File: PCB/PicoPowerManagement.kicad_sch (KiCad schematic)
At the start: 17 parts, among them J1 UART Header, J2 DEBUG, J3 SwitchLEDS, J4 PowerSwitch, J5 NAS Fan 1, J6 NAS Fan 2, J7 ATX 24P Connection, Q1 2N3904, U2 LP5810ADSDR, U3 LP5810ADSDR, U4 LSF0101DRYR, U5 LSF0101DRYR

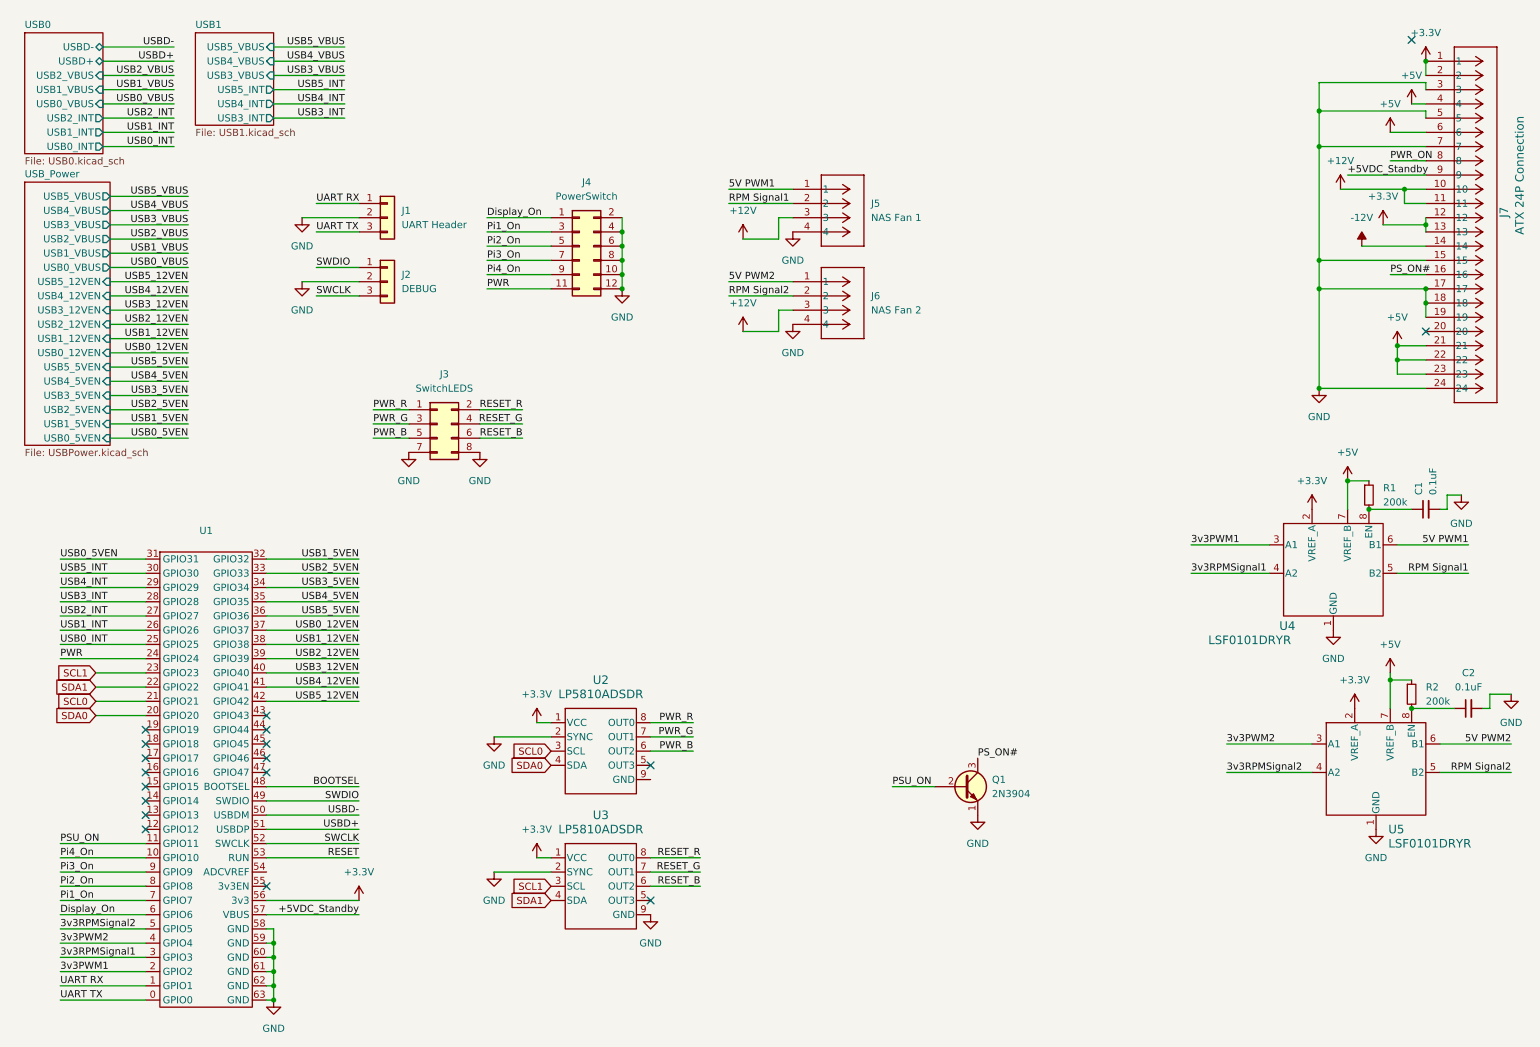
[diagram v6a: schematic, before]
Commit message: Add 2N3904 component library and update footprint and symbol definitions
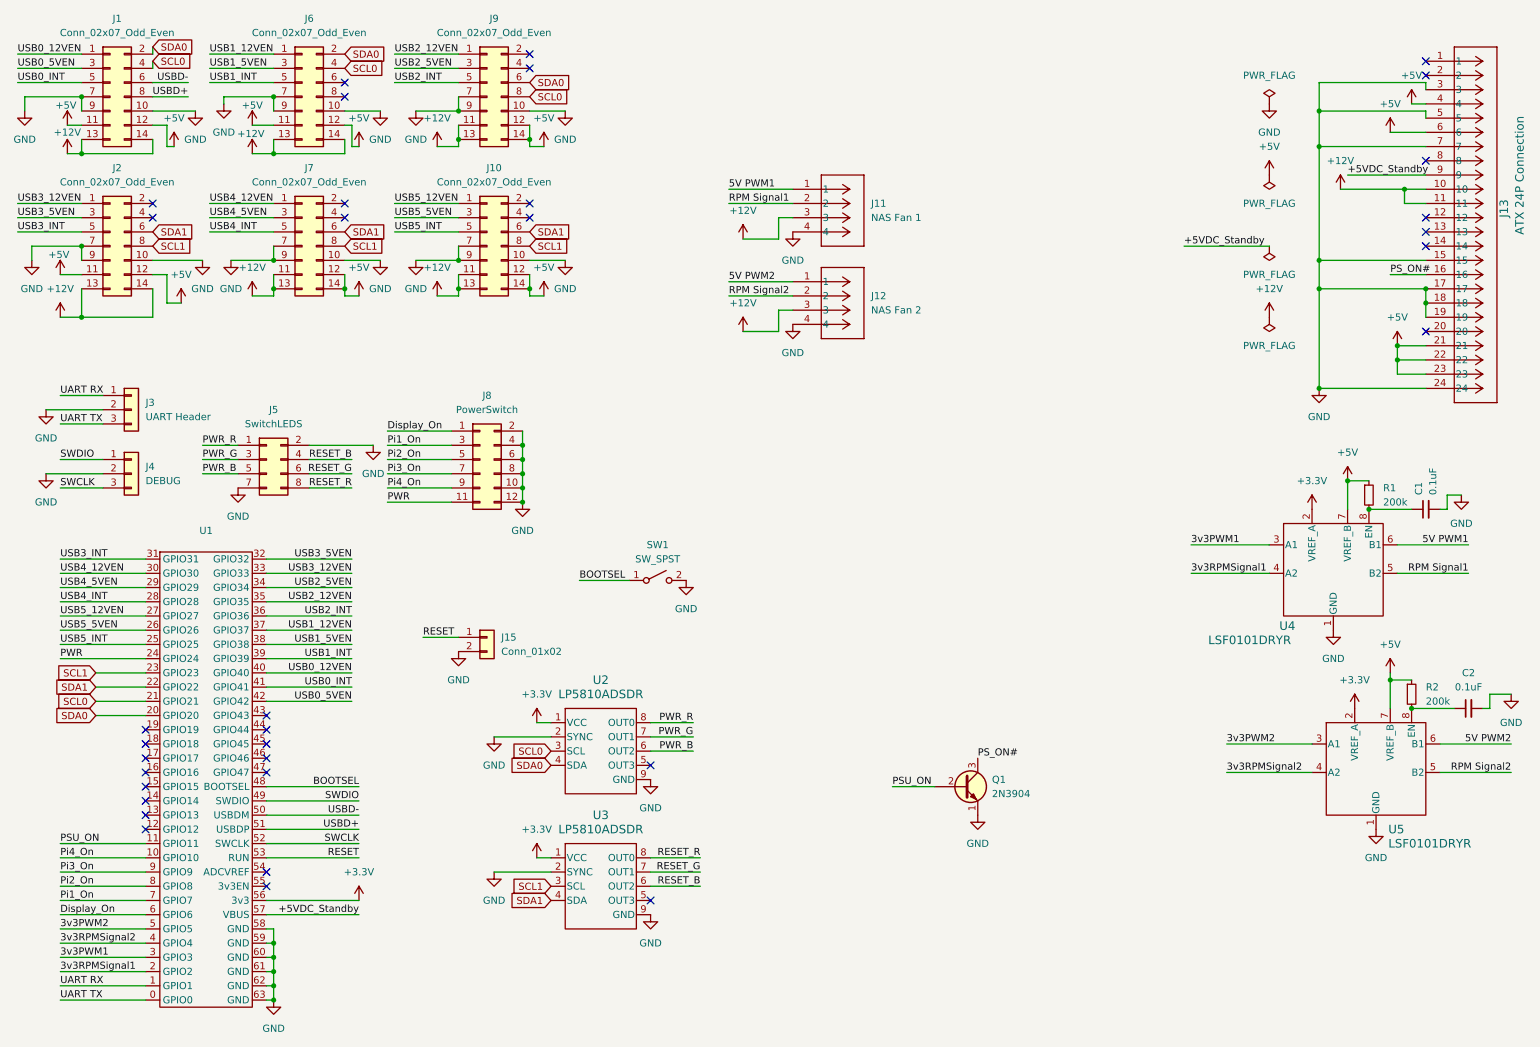
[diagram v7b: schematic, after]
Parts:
- added J1, J10, J2, J6, J7, J9: Conn_02x07_Odd_Even, Connector_PinHeader_2.54mm:PinHeader_2x07_P2.54mm_Vertical, symbol Connector_Generic:Conn_02x07_Odd_Even
- added J15: Conn_01x02, Connector_PinHeader_2.54mm:PinHeader_1x02_P2.54mm_Vertical, symbol Connector_Generic:Conn_01x02
- added SW1: SW_SPST, Button_Switch_SMD:Panasonic_EVQPUJ_EVQPUA, symbol Switch:SW_SPST
- Q1: footprint Package_TO_SOT_THT:TO-92-2_Wide -> 2N3904:TO92254P460H750-3
- renumbered J5 to J11, J6 to J12, J7 to J13, J1 to J3, J2 to J4, J3 to J5, J4 to J8
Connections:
- net +12V: now also J1.13 (Pin_13), J1.14 (Pin_14), J10.11 (Pin_11), J10.13 (Pin_13), J2.13 (Pin_13), J2.14 (Pin_14), J6.13 (Pin_13), J6.14 (Pin_14), J7.11 (Pin_11), J7.13 (Pin_13), J9.11 (Pin_11), J9.13 (Pin_13)
- net +3.3V: no longer J13.1, J13.12, J13.13, J13.2
- net +5V: now also J1.11 (Pin_11), J1.12 (Pin_12), J10.12 (Pin_12), J10.14 (Pin_14), J2.11 (Pin_11), J2.12 (Pin_12), J6.11 (Pin_11), J6.12 (Pin_12), J7.12 (Pin_12), J7.14 (Pin_14), J9.12 (Pin_12), J9.14 (Pin_14)
- net 3v3PWM1: now also U1.3 (GPIO3); no longer U1.2 (GPIO2)
- net 3v3PWM2: now also U1.5 (GPIO5); no longer U1.4 (GPIO4)
- net 3v3RPMSignal1: now also U1.2 (GPIO2); no longer U1.3 (GPIO3)
- net 3v3RPMSignal2: now also U1.4 (GPIO4); no longer U1.5 (GPIO5)
- net BOOTSEL: now also SW1.1 (A)
- net GND: now also J5.2 (Pin_2), U2.9 (GND), J1.10 (Pin_10), J1.7 (Pin_7), J1.9 (Pin_9), J10.10 (Pin_10), J10.7 (Pin_7), J10.9 (Pin_9), J15.2 (Pin_2), J2.10 (Pin_10), J2.7 (Pin_7), J2.9 (Pin_9), J6.10 (Pin_10), J6.7 (Pin_7), J6.9 (Pin_9), J7.10 (Pin_10), J7.7 (Pin_7), J7.9 (Pin_9), J9.10 (Pin_10), J9.7 (Pin_7), J9.9 (Pin_9), SW1.2 (B); no longer J5.8 (Pin_8)
- net RESET: now also J15.1 (Pin_1)
- net RESET_B: now also J5.4 (Pin_4); no longer J5.6 (Pin_6)
- net RESET_G: now also J5.6 (Pin_6); no longer J5.4 (Pin_4)
- net RESET_R: now also J5.8 (Pin_8); no longer J5.2 (Pin_2)
- net SCL0: now also J1.4 (Pin_4), J6.4 (Pin_4), J9.8 (Pin_8)
- net SCL1: now also J10.8 (Pin_8), J2.8 (Pin_8), J7.8 (Pin_8)
- net SDA0: now also J1.2 (Pin_2), J6.2 (Pin_2), J9.6 (Pin_6)
- net SDA1: now also J10.6 (Pin_6), J2.6 (Pin_6), J7.6 (Pin_6)
- net USB0_12VEN: now also U1.40 (GPIO40), J1.1 (Pin_1); no longer U1.37 (GPIO37)
- net USB0_5VEN: now also U1.42 (GPIO42), J1.3 (Pin_3); no longer U1.31 (GPIO31)
- net USB0_INT: now also U1.41 (GPIO41), J1.5 (Pin_5); no longer U1.25 (GPIO25)
- net USB1_12VEN: now also U1.37 (GPIO37), J6.1 (Pin_1); no longer U1.38 (GPIO38)
- net USB1_5VEN: now also U1.38 (GPIO38), J6.3 (Pin_3); no longer U1.32 (GPIO32)
- net USB1_INT: now also U1.39 (GPIO39), J6.5 (Pin_5); no longer U1.26 (GPIO26)
- net USB2_12VEN: now also U1.35 (GPIO35), J9.1 (Pin_1); no longer U1.39 (GPIO39)
- net USB2_5VEN: now also U1.34 (GPIO34), J9.3 (Pin_3); no longer U1.33 (GPIO33)
- net USB2_INT: now also U1.36 (GPIO36), J9.5 (Pin_5); no longer U1.27 (GPIO27)
- net USB3_12VEN: now also U1.33 (GPIO33), J2.1 (Pin_1); no longer U1.40 (GPIO40)
- net USB3_5VEN: now also U1.32 (GPIO32), J2.3 (Pin_3); no longer U1.34 (GPIO34)
- net USB3_INT: now also U1.31 (GPIO31), J2.5 (Pin_5); no longer U1.28 (GPIO28)
- net USB4_12VEN: now also U1.30 (GPIO30), J7.1 (Pin_1); no longer U1.41 (GPIO41)
- net USB4_5VEN: now also U1.29 (GPIO29), J7.3 (Pin_3); no longer U1.35 (GPIO35)
- net USB4_INT: now also U1.28 (GPIO28), J7.5 (Pin_5); no longer U1.29 (GPIO29)
- net USB5_12VEN: now also U1.27 (GPIO27), J10.1 (Pin_1); no longer U1.42 (GPIO42)
- net USB5_5VEN: now also U1.26 (GPIO26), J10.3 (Pin_3); no longer U1.36 (GPIO36)
- net USB5_INT: now also U1.25 (GPIO25), J10.5 (Pin_5); no longer U1.30 (GPIO30)
- net USBD+: now also J1.8 (Pin_8)
- net USBD-: now also J1.6 (Pin_6)
- net -12V: no longer names the net of J13.14
- net PWR_ON: no longer names the net of J13.8
- no-connect marks 18 -> 34
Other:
- removed sheet USB0
- removed sheet USB1
- removed sheet USB_Power
- moved on the sheet: J3, J4, J5, J8

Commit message: confused now
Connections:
- net +12V: now also J1.2 (Pin_2), J1.4 (Pin_4), J2.1 (Pin_1), J2.3 (Pin_3), J6.1 (Pin_1), J6.3 (Pin_3); no longer J1.13 (Pin_13), J1.14 (Pin_14), J2.13 (Pin_13), J2.14 (Pin_14), J6.13 (Pin_13), J6.14 (Pin_14)
- net +3.3V: now also J1.14 (Pin_14), J2.14 (Pin_14), J6.14 (Pin_14)
- net +5V: now also J1.1 (Pin_1), J1.3 (Pin_3), J2.2 (Pin_2), J2.4 (Pin_4), J6.2 (Pin_2), J6.4 (Pin_4); no longer J1.11 (Pin_11), J1.12 (Pin_12), J2.11 (Pin_11), J2.12 (Pin_12), J6.11 (Pin_11), J6.12 (Pin_12)
- net GND: now also J1.5 (Pin_5), J1.6 (Pin_6), J2.5 (Pin_5), J2.6 (Pin_6), J6.5 (Pin_5), J6.6 (Pin_6); no longer J1.10 (Pin_10), J1.7 (Pin_7), J1.9 (Pin_9), J2.10 (Pin_10), J2.7 (Pin_7), J2.9 (Pin_9), J6.10 (Pin_10), J6.7 (Pin_7), J6.9 (Pin_9)
- net SCL0: now also J1.12 (Pin_12), J6.12 (Pin_12); no longer J1.4 (Pin_4), J6.4 (Pin_4)
- net SCL1: now also J2.12 (Pin_12); no longer J2.8 (Pin_8)
- net SDA0: now also J1.10 (Pin_10), J6.10 (Pin_10); no longer J1.2 (Pin_2), J6.2 (Pin_2)
- net SDA1: now also J2.10 (Pin_10); no longer J2.6 (Pin_6)
- net USB0_12VEN: now also J1.8 (Pin_8); no longer J1.1 (Pin_1)
- net USB0_5VEN: now also J1.7 (Pin_7); no longer J1.3 (Pin_3)
- net USB0_INT: now also J1.9 (Pin_9); no longer J1.5 (Pin_5)
- net USB1_12VEN: now also J6.8 (Pin_8); no longer J6.1 (Pin_1)
- net USB1_5VEN: now also J6.7 (Pin_7); no longer J6.3 (Pin_3)
- net USB1_INT: now also J6.9 (Pin_9); no longer J6.5 (Pin_5)
- net USB3_12VEN: now also J2.8 (Pin_8); no longer J2.1 (Pin_1)
- net USB3_5VEN: now also J2.7 (Pin_7); no longer J2.3 (Pin_3)
- net USB3_INT: now also J2.9 (Pin_9); no longer J2.5 (Pin_5)
- net USBD+: now also J1.11 (Pin_11); no longer J1.8 (Pin_8)
- net USBD-: now also J1.13 (Pin_13); no longer J1.6 (Pin_6)
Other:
- moved on the sheet: J1, J10, J2, J6, J7, J9
